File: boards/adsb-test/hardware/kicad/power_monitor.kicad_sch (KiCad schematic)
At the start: 0 parts

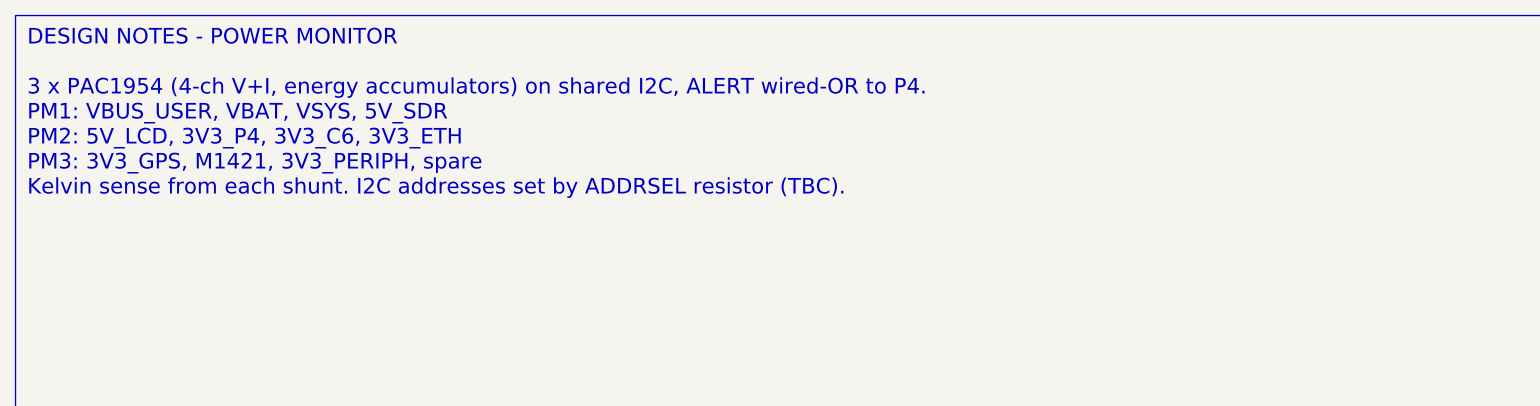
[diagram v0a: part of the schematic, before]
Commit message: Release v0.4.0: ADSB_Test with ESP32-C5, ADSBee m1421 and LA5016 header
- C6 -> C5 co-processor; m1421 identified and integrated (symbol/footprint
  from the ADSBee 1421 carrier, GPL-3.0 attribution)
- Power budget and 2S1P battery sizing for >= 1 h; USB-A for 1-2 SDRs via hub
- Dev port: FT2232H + RP2040 debugprobe; TCA6408A expander for slow I/O
- Test Debug sheet with LA5016 header and rail test points
- Vendor documents git-ignored (public repo)

Co-Authored-By: Claude Opus 5.5 <noreply@anthropic.com>
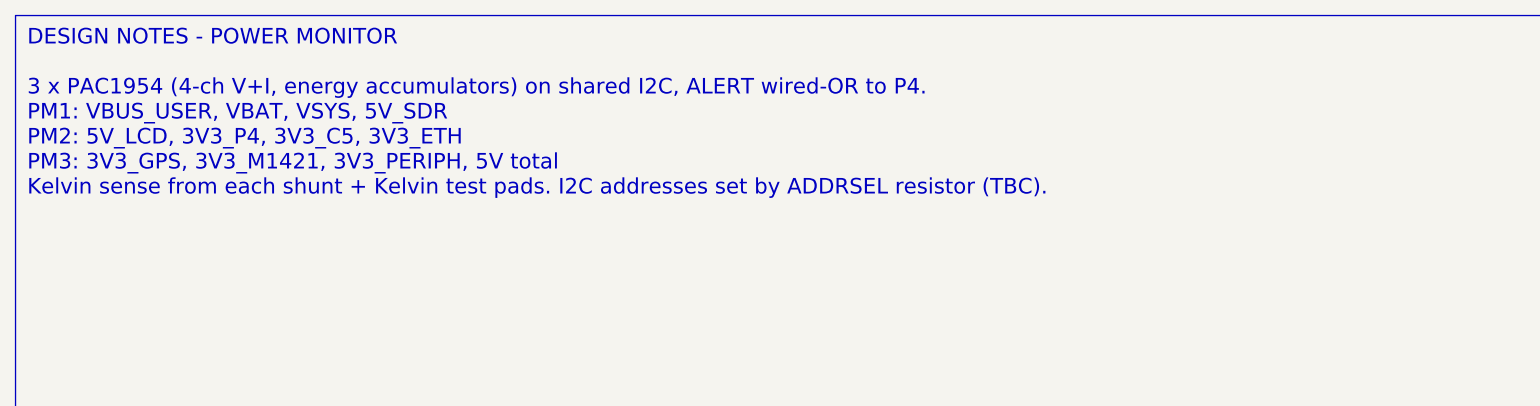
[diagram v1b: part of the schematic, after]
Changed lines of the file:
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@@
 		(comment 1 "Requirements: boards/adsb-test/docs/requirements.md")
 	)
-	(text_box "DESIGN NOTES - POWER MONITOR\n\n3 x PAC1954 (4-ch V+I, energy accumulators) on shared I2C, ALERT wired-OR to P4.\nPM1: VBUS_USER, VBAT, VSYS, 5V_SDR\nPM2: 5V_LCD, 3V3_P4, 3V3_C6, 3V3_ETH\nPM3: 3V3_GPS, M1421, 3V3_PERIPH, spare\nKelvin sense from each shunt. I2C addresses set by ADDRSEL resistor (TBC)."
+	(text_box "DESIGN NOTES - POWER MONITOR\n\n3 x PAC1954 (4-ch V+I, energy accumulators) on shared I2C, ALERT wired-OR to P4.\nPM1: VBUS_USER, VBAT, VSYS, 5V_SDR\nPM2: 5V_LCD, 3V3_P4, 3V3_C5, 3V3_ETH\nPM3: 3V3_GPS, 3V3_M1421, 3V3_PERIPH, 5V total\nKelvin sense from each shunt + Kelvin test pads. I2C addresses set by ADDRSEL resistor (TBC)."
 		(exclude_from_sim no)
 		(at 20 20 0)

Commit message: Release v0.17.0: ADSB_Test power schematics (PD input, 2S charger, rails, monitors)
Co-Authored-By: Claude Opus 5.5 <noreply@anthropic.com>
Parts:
- added C501, C502, C503: 100nF, Capacitor_SMD:C_0402_1005Metric, symbol Device:C
- added R501: TBC (PM1), Resistor_SMD:R_0402_1005Metric, symbol Device:R
- added R502: TBC (PM2), Resistor_SMD:R_0402_1005Metric, symbol Device:R
- added R503: TBC (PM3), Resistor_SMD:R_0402_1005Metric, symbol Device:R
- added R504: 10k, Resistor_SMD:R_0402_1005Metric, symbol Device:R
- added U501: PAC1954 (PM1), Package_DFN_QFN:VQFN-16-1EP_3x3mm_P0.5mm_EP1.1x1.1mm, symbol Sensor_Energy:PAC1954x-x4MX
- added U502: PAC1954 (PM2), Package_DFN_QFN:VQFN-16-1EP_3x3mm_P0.5mm_EP1.1x1.1mm, symbol Sensor_Energy:PAC1954x-x4MX
- added U503: PAC1954 (PM3), Package_DFN_QFN:VQFN-16-1EP_3x3mm_P0.5mm_EP1.1x1.1mm, symbol Sensor_Energy:PAC1954x-x4MX
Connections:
- new net 3V3_PERIPH: C501.1, C502.1, C503.1, R504.1, U501.16 (~{PWRDN}), U501.2 (V_{DD}), U502.16 (~{PWRDN}), U502.2 (V_{DD}), U503.16 (~{PWRDN}), U503.2 (V_{DD})
- new net GND: C501.2, C502.2, C503.2, R501.2, R502.2, R503.2, U501.1 (SLOW), U501.17 (EP), U501.3 (GND), U502.1 (SLOW), U502.17 (EP), U502.3 (GND), U503.1 (SLOW), U503.17 (EP), U503.3 (GND)
- new net I2C_SCL: U501.4 (SCL), U502.4 (SCL), U503.4 (SCL)
- new net I2C_SDA: U501.5 (SDA), U502.5 (SDA), U503.5 (SDA)
- new net PM1_ADDR: R501.1, U501.6 (ADDRSEL)
- new net PM1_CH1_N: U501.12 (SENSE1-)
- new net PM1_CH1_P: U501.11 (SENSE1+)
- new net PM1_CH2_N: U501.14 (SENSE2-)
- new net PM1_CH2_P: U501.13 (SENSE2+)
- new net PM1_CH3_N: U501.7 (SENSE3-)
- new net PM1_CH3_P: U501.8 (SENSE3+)
- new net PM1_CH4_N: U501.9 (SENSE4-)
- new net PM1_CH4_P: U501.10 (SENSE4+)
- new net PM2_ADDR: R502.1, U502.6 (ADDRSEL)
- new net PM2_CH1_N: U502.12 (SENSE1-)
- new net PM2_CH1_P: U502.11 (SENSE1+)
- new net PM2_CH2_N: U502.14 (SENSE2-)
- new net PM2_CH2_P: U502.13 (SENSE2+)
- new net PM2_CH3_N: U502.7 (SENSE3-)
- new net PM2_CH3_P: U502.8 (SENSE3+)
- new net PM2_CH4_N: U502.9 (SENSE4-)
- new net PM2_CH4_P: U502.10 (SENSE4+)
- new net PM3_ADDR: R503.1, U503.6 (ADDRSEL)
- new net PM3_CH1_N: U503.12 (SENSE1-)
- new net PM3_CH1_P: U503.11 (SENSE1+)
- new net PM3_CH2_N: U503.14 (SENSE2-)
- new net PM3_CH2_P: U503.13 (SENSE2+)
- new net PM3_CH3_N: U503.7 (SENSE3-)
- new net PM3_CH3_P: U503.8 (SENSE3+)
- new net PM3_CH4_N: U503.9 (SENSE4-)
- new net PM3_CH4_P: U503.10 (SENSE4+)
- new net PM_ALERT: R504.2, U501.15 (GPIO), U502.15 (GPIO), U503.15 (GPIO)
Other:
- note added: "PM1: CH1 VBUS_USER, CH2 VBAT (bidirectional), CH3 VSYS, CH4 5V_SDR PM2: CH1 5V_LCD, CH2 3V3_P4, CH3 3V3_C5, CH4 3V3_ETH PM3: CH1 3V3_GPS, CH2 3V3_M1421, CH3 3V3_PERIPH, CH4 3V3 total Sense lines: Kelvin from each shunt (pins 2/3), routed as pairs."

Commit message: Release v0.18.0: power switch, always-on VBACKUP, hand-solder footprints, PCBWay notes
Co-Authored-By: Claude Opus 5.5 <noreply@anthropic.com>
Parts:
- C501, C502, C503: footprint Capacitor_SMD:C_0402_1005Metric -> Capacitor_SMD:C_0805_2012Metric_Pad1.18x1.45mm_HandSolder
- R501, R502, R503, R504: footprint Resistor_SMD:R_0402_1005Metric -> Resistor_SMD:R_0805_2012Metric_Pad1.20x1.40mm_HandSolder

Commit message: Release v0.19.0: hand-solder footprints (m1421, QFNs, SOT-23, SO-8), Rev 1 hand assembly
Co-Authored-By: Claude Opus 5.5 <noreply@anthropic.com>
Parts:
- R501: value TBC (PM1) -> 0R (0x10)
- R502: value TBC (PM2) -> 499R 1% (0x11)
- R503: value TBC (PM3) -> 806R 1% (0x12)
- U501: footprint Package_DFN_QFN:VQFN-16-1EP_3x3mm_P0.5mm_EP1.1x1.1mm -> ADSB_Test:VQFN-16-1EP_3x3mm_P0.5mm_EP1.1x1.1mm_HandSolder; Check ADDRSEL resistor value sets the I2C address: TBC vs Microch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 -> (none); I2C (none) -> 0x10 (ADDRSEL, DS20006539 Table 6-1)
- U502: footprint Package_DFN_QFN:VQFN-16-1EP_3x3mm_P0.5mm_EP1.1x1.1mm -> ADSB_Test:VQFN-16-1EP_3x3mm_P0.5mm_EP1.1x1.1mm_HandSolder; Check ADDRSEL resistor value sets the I2C address: TBC vs Microch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 -> (none); I2C (none) -> 0x11 (ADDRSEL, DS20006539 Table 6-1)
- U503: footprint Package_DFN_QFN:VQFN-16-1EP_3x3mm_P0.5mm_EP1.1x1.1mm -> ADSB_Test:VQFN-16-1EP_3x3mm_P0.5mm_EP1.1x1.1mm_HandSolder; Check ADDRSEL resistor value sets the I2C address: TBC vs Microch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 -> (none); I2C (none) -> 0x12 (ADDRSEL, DS20006539 Table 6-1)

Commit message: Release v0.21.0: WT01P4C5-S1 module (P4+C5) and DS3231M RTC for ADSB_Test
Co-Authored-By: Claude Opus 5.5 <noreply@anthropic.com>
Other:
- note added: "PM1: CH1 VBUS_USER, CH2 VBAT (bidirectional), CH3 VSYS, CH4 5V_SDR PM2: CH1 5V_LCD, CH2 5V_MCU (P4+C5 module), CH3 3V3_SD, CH4 3V3_ETH PM3: CH1 3V3_GPS, CH2 3V3_M1421, CH3 3V3_PERIPH, CH4 3V3 total Sense lines: Kelvin from each shunt (pins 2/3), routed as pairs."
- note removed: "PM1: CH1 VBUS_USER, CH2 VBAT (bidirectional), CH3 VSYS, CH4 5V_SDR PM2: CH1 5V_LCD, CH2 3V3_P4, CH3 3V3_C5, CH4 3V3_ETH PM3: CH1 3V3_GPS, CH2 3V3_M1421, CH3 3V3_PERIPH, CH4 3V3 total Sense lines: Kelvin from each shunt (pins 2/3), routed as pairs."

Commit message: Release v0.24.0: OSPTEK ESP32-P4C5 Core module replaces WT01P4C5-S1
Co-Authored-By: Claude Opus 5.5 <noreply@anthropic.com>
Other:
- note added: "PM1: CH1 VBUS_USER, CH2 VBAT (bidirectional), CH3 VSYS, CH4 5V_SDR PM2: CH1 5V_LCD, CH2 3V3_MCU (P4+C5 module), CH3 3V3_SD, CH4 3V3_ETH PM3: CH1 3V3_GPS, CH2 3V3_M1421, CH3 3V3_PERIPH, CH4 3V3 total Sense lines: Kelvin from each shunt (pins 2/3), routed as pairs."
- note removed: "PM1: CH1 VBUS_USER, CH2 VBAT (bidirectional), CH3 VSYS, CH4 5V_SDR PM2: CH1 5V_LCD, CH2 5V_MCU (P4+C5 module), CH3 3V3_SD, CH4 3V3_ETH PM3: CH1 3V3_GPS, CH2 3V3_M1421, CH3 3V3_PERIPH, CH4 3V3 total Sense lines: Kelvin from each shunt (pins 2/3), routed as pairs."
